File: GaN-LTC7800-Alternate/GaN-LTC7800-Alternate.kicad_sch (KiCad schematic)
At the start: 40 parts, among them Q1 EPC2014C, Q2 EPC2014C, U1 LTC7800HUDC_PBF

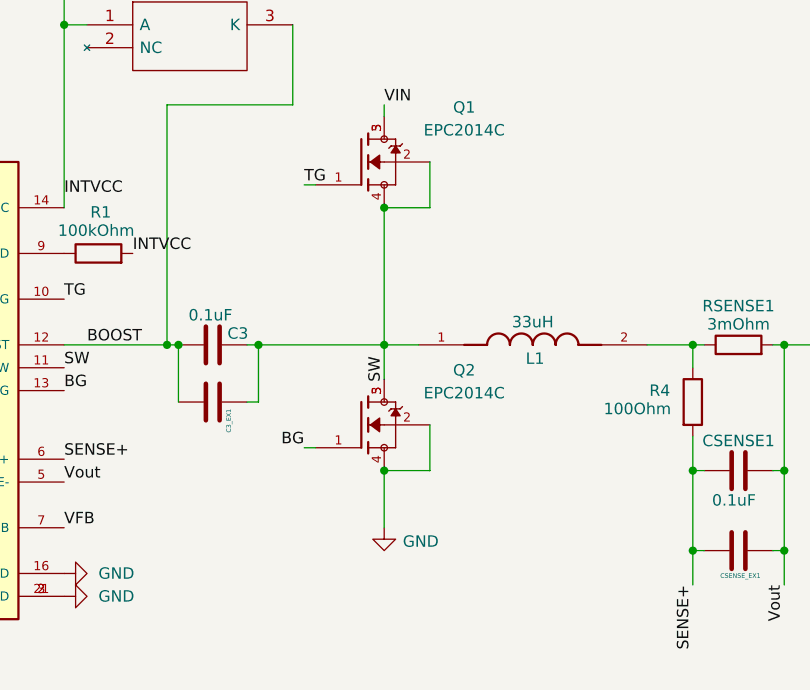
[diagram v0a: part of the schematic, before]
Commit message: new GaN switches, added alt projects
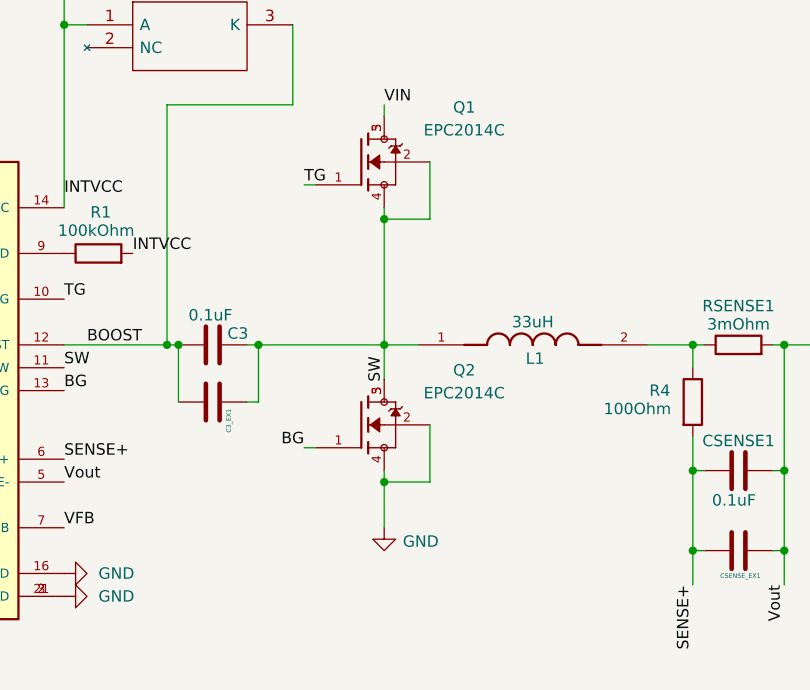
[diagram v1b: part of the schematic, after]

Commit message: Updated for preassembly
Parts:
- added RLOAD2: 2Ohm, Resistor_SMD:R_0201_0603Metric, symbol Device:R
- C1, C3, CSENSE1: footprint Capacitor_SMD:C_0805_2012Metric_Pad1.18x1.45mm_HandSolder -> Capacitor_SMD:C_0805_2012Metric; LCSC (none) -> C49678
- C2, C5, CinA1, CinA2: footprint Capacitor_SMD:C_0805_2012Metric_Pad1.18x1.45mm_HandSolder -> Capacitor_SMD:C_0805_2012Metric; LCSC (none) -> C19110
- C6: footprint Capacitor_SMD:C_0805_2012Metric_Pad1.18x1.45mm_HandSolder -> Capacitor_SMD:C_0805_2012Metric; LCSC (none) -> C1970
- COUT1: footprint Capacitor_SMD:C_0805_2012Metric_Pad1.18x1.45mm_HandSolder -> Capacitor_SMD:C_0805_2012Metric; LCSC (none) -> C141660
- CinB1: footprint Capacitor_SMD:C_0805_2012Metric_Pad1.18x1.45mm_HandSolder -> Capacitor_Tantalum_SMD:CP_EIA-7343-31_Kemet-D; LCSC (none) -> C465937
- D1: LCSC (none) -> C17357273
- R1: footprint Resistor_SMD:R_0201_0603Metric_Pad0.64x0.40mm_HandSolder -> Resistor_SMD:R_0201_0603Metric; LCSC (none) -> C14675
- R2: footprint Resistor_SMD:R_0201_0603Metric_Pad0.64x0.40mm_HandSolder -> Resistor_SMD:R_0201_0603Metric; LCSC (none) -> C861257
- R4: footprint Resistor_SMD:R_0201_0603Metric_Pad0.64x0.40mm_HandSolder -> Resistor_SMD:R_0201_0603Metric; LCSC (none) -> C105588
- R5: footprint Resistor_SMD:R_0201_0603Metric_Pad0.64x0.40mm_HandSolder -> Resistor_SMD:R_0201_0603Metric; LCSC (none) -> C2907055
- R6: footprint Resistor_SMD:R_0201_0603Metric_Pad0.64x0.40mm_HandSolder -> Resistor_SMD:R_0201_0603Metric; LCSC (none) -> C2907008
- R7: footprint Resistor_SMD:R_0201_0603Metric_Pad0.64x0.40mm_HandSolder -> Resistor_SMD:R_0201_0603Metric; LCSC (none) -> C2907028
- R9: footprint Resistor_SMD:R_0201_0603Metric_Pad0.64x0.40mm_HandSolder -> Resistor_SMD:R_0201_0603Metric; LCSC (none) -> C4168160
- RLOAD1: value 5Ohm -> 3Ohm; footprint Resistor_SMD:R_0201_0603Metric_Pad0.64x0.40mm_HandSolder -> Resistor_SMD:R_0201_0603Metric; LCSC (none) -> C23157
- RSENSE1: footprint Resistor_SMD:R_0201_0603Metric_Pad0.64x0.40mm_HandSolder -> Resistor_SMD:R_0201_0603Metric; LCSC (none) -> C7256520
- U1: LCSC (none) -> C690192
- VSource_GND1, VSource_IN1: LCSC (none) -> C4944061
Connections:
- net GND: now also RLOAD2.2; no longer RLOAD1.2
- new net: RLOAD1.2, RLOAD2.1
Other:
- moved on the sheet: C1, C1_EX1, C2, C2_EX1, C3, C3_EX1, C5, C5_EX1, C6, C6_EX1, COUT1, COUT_EX1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
